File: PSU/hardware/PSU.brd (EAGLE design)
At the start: 143.5 x 58.5 mm, 202 parts, among them J1 SWD, J2 UART, Q1 PMOS-DPAK, Q10 PMOS-SOT23, Q11 NPN, Q2 PMOS-SOT23, Q3 NPN, Q4 PMOS-SOT23, Q5 NMOS-SOT23, Q6 PMOS-DPAK, Q7 PMOS-SOT23, Q8 NMOS-SOT23, Q9 PMOS-DPAK, U1 LM2576, U10 4069, U11 LTV-247, U12 74HC08, U13 STM8S003K3T6C, U14 74HC08, U15 4051, U16 358, U17 358, U18 74HC32, U2 MT3608, U3 7805, U4 324, U5 MC34063, U6 MT3608, U7 LM2576, U8 MC34063, U9 TP4056

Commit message: [HW/PSU] Fix backup regulator enabling
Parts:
- added Q12: PMOS-SOT23, SparkFun-DiscreteSemi:SOT23-3
- moved C12 0.63 mm to (41.3, 47.6)
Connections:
- new net VBACKUP_SW: C12.1, L4.1, Q12.3, U6.4, U6.5
- net MEM_BACKUP: now also Q12.1; no longer U6.4
- net VBACKUP: now also Q12.2; no longer C12.1, L4.1, U6.5
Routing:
- net VBACKUP: track 190.6 -> 175.9 mm, vias 4 -> 3
- net VBACKUP_SW: track 0.00 -> 12.8 mm, vias 0 -> 1
- net MEM_BACKUP: track 21.8 -> 16.5 mm
- net VCCIO: track 181.9 -> 180.4 mm
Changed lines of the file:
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@@
 <attribute name="SPICEPREFIX" value="R" x="46.355" y="19.05" size="0.254" layer="156" font="vector" ratio="10" rot="MR180" display="off"/>
 </element>
-<element name="C12" library="rcl" library_urn="urn:adsk.eagle:library:334" package="C1206" package3d_urn="urn:adsk.eagle:package:23618/2" value="10u" x="40.64" y="47.625" smashed="yes" rot="MR90">
-<attribute name="NAME" x="40.64" y="44.958" size="0.8128" layer="26" font="vector" ratio="10" rot="MR180" align="bottom-center"/>
-<attribute name="POPULARITY" value="54" x="44.45" y="36.195" size="0.254" layer="156" font="vector" ratio="10" rot="MR90" display="off"/>
-<attribute name="SPICEPREFIX" value="C" x="44.45" y="36.195" size="0.254" layer="156" font="vector" ratio="10" rot="MR90" display="off"/>
+<element name="C12" library="rcl" library_urn="urn:adsk.eagle:library:334" package="C1206" package3d_urn="urn:adsk.eagle:package:23618/2" value="10u" x="41.275" y="47.625" smashed="yes" rot="MR90">
+<attribute name="NAME" x="41.275" y="44.958" size="0.8128" layer="26" font="vector" ratio="10" rot="MR180" align="bottom-center"/>
+<attribute name="POPULARITY" value="54" x="45.085" y="36.195" size="0.254" layer="156" font="vector" ratio="10" rot="MR90" display="off"/>
+<attribute name="SPICEPREFIX" value="C" x="45.085" y="36.195" size="0.254" layer="156" font="vector" ratio="10" rot="MR90" display="off"/>
 </element>
 <element name="D9" library="custom" package="DO-214AC" value="SS14" x="52.07" y="46.99" smashed="yes" rot="MR0">
@@
 <attribute name="TP_SIGNAL_NAME" value="" x="48.895" y="18.415" size="0.254" layer="156" font="vector" ratio="10"/>
 </element>
+<element name="Q12" library="SparkFun-DiscreteSemi" package="SOT23-3" value="PMOS-SOT23" x="38.1" y="46.99" smashed="yes" rot="MR180">
+<attribute name="NAME" x="38.1" y="45.085" size="0.8128" layer="26" font="vector" ratio="10" rot="MR180" align="bottom-center"/>
+<attribute name="PROD_ID" value="TRANS-11153" x="38.1" y="46.99" size="1.778" layer="28" rot="MR180" display="off"/>
+<attribute name="VALUE" x="39.751" y="46.99" size="0.6096" layer="28" font="vector" ratio="20" rot="MR270" align="top-center"/>
+</element>
 </elements>
 <signals>
@@
 <contactref element="U9" pad="5"/>
 <contactref element="PJ3" pad="1"/>
-<contactref element="U6" pad="5"/>
-<contactref element="C12" pad="1"/>
 <contactref element="D4" pad="A"/>
 <contactref element="U15" pad="12"/>
 <contactref element="C22" pad="1"/>
-<contactref element="L4" pad="1"/>
-<via x="37.465" y="53.34" extent="1-16" drill="0.35" shape="octagon"/>
-<via x="43.18" y="46.355" extent="1-16" drill="0.35" shape="octagon"/>
-<via x="46.99" y="53.34" extent="1-16" drill="0.35" shape="octagon"/>
 <via x="97.79" y="21.844" extent="1-16" drill="0.35" shape="octagon"/>
-<wire x1="37.465" y1="53.34" x2="46.99" y2="53.34" width="0.4064" layer="16"/>
-<wire x1="46.99" y1="53.34" x2="86.995" y2="53.34" width="0.4064" layer="16"/>
+<wire x1="48.895" y1="53.34" x2="86.995" y2="53.34" width="0.4064" layer="16"/>
 <wire x1="86.995" y1="53.34" x2="89.535" y2="55.88" width="0.4064" layer="16"/>
 <wire x1="89.535" y1="55.88" x2="96.52" y2="55.88" width="0.4064" layer="16"/>
@@
 <wire x1="108.08" y1="45.85" x2="109.22" y2="46.99" width="0.4064" layer="16"/>
 <wire x1="109.22" y1="44.9834" x2="109.22" y2="46.99" width="0.4064" layer="16"/>
-<wire x1="46.355" y1="50.165" x2="43.285" y2="50.165" width="0.4064" layer="1"/>
-<wire x1="43.18" y1="46.355" x2="43.18" y2="50.06" width="0.4064" layer="1"/>
-<wire x1="43.18" y1="50.06" x2="43.285" y2="50.165" width="0.4064" layer="1"/>
-<wire x1="46.355" y1="50.165" x2="46.99" y2="50.8" width="0.4064" layer="1"/>
-<wire x1="46.99" y1="50.8" x2="46.99" y2="53.34" width="0.4064" layer="1"/>
-<wire x1="46.99" y1="53.34" x2="65.405" y2="53.34" width="0.4064" layer="1"/>
+<wire x1="48.895" y1="53.34" x2="65.405" y2="53.34" width="0.4064" layer="1"/>
 <wire x1="65.405" y1="53.34" x2="67.31" y2="51.435" width="0.4064" layer="1"/>
 <wire x1="67.31" y1="51.435" x2="67.31" y2="34.925" width="0.4064" layer="1"/>
@@
 <wire x1="97.79" y1="24.765" x2="97.155" y2="25.4" width="0.4064" layer="1"/>
 <wire x1="88.265" y1="25.4" x2="97.155" y2="25.4" width="0.4064" layer="1"/>
-<wire x1="44.9799" y1="47.625" x2="43.815" y2="47.625" width="0.4064" layer="16"/>
-<wire x1="43.815" y1="47.625" x2="43.18" y2="46.99" width="0.4064" layer="16"/>
-<wire x1="43.18" y1="46.99" x2="43.18" y2="46.355" width="0.4064" layer="16"/>
 <wire x1="97.79" y1="21.844" x2="97.79" y2="24.0284" width="0.4064" layer="16"/>
 <wire x1="69.85" y1="32.385" x2="82.55" y2="32.385" width="0.4064" layer="1"/>
@@
 <wire x1="84.455" y1="28.575" x2="85.09" y2="28.575" width="0.4064" layer="1"/>
 <wire x1="85.09" y1="28.575" x2="88.265" y2="25.4" width="0.4064" layer="1"/>
-<wire x1="40.64" y1="46.225" x2="41.78" y2="46.225" width="0.4064" layer="16"/>
-<wire x1="41.78" y1="46.225" x2="41.91" y2="46.355" width="0.4064" layer="16"/>
-<wire x1="41.91" y1="46.355" x2="43.18" y2="46.355" width="0.4064" layer="16"/>
+<contactref element="Q12" pad="2"/>
+<wire x1="39.05" y1="47.99" x2="39.64" y2="47.99" width="0.4064" layer="16"/>
+<wire x1="39.64" y1="47.99" x2="40.005" y2="47.625" width="0.4064" layer="16"/>
+<wire x1="40.005" y1="47.625" x2="42.545" y2="47.625" width="0.4064" layer="16"/>
+<wire x1="42.545" y1="47.625" x2="43.18" y2="48.26" width="0.4064" layer="16"/>
+<wire x1="43.18" y1="48.26" x2="43.18" y2="48.895" width="0.4064" layer="16"/>
+<wire x1="44.4274" y1="50.1424" x2="48.26" y2="50.1424" width="0.4064" layer="16"/>
+<wire x1="43.18" y1="48.895" x2="44.4274" y2="50.1424" width="0.4064" layer="16"/>
+<via x="48.26" y="50.1424" extent="1-16" drill="0.35" shape="octagon"/>
+<via x="48.895" y="53.34" extent="1-16" drill="0.35" shape="octagon"/>
+<wire x1="48.895" y1="53.34" x2="48.26" y2="52.705" width="0.4064" layer="1"/>
+<wire x1="48.26" y1="52.705" x2="48.26" y2="50.1424" width="0.4064" layer="1"/>
 </signal>
 <signal name="^CHG_CTRL" class="1">
@@
 <contactref element="U10" pad="9"/>
 <wire x1="81.915" y1="26.5684" x2="81.915" y2="27.94" width="0.254" layer="1"/>
-<wire x1="80.645" y1="28.575" x2="80.01" y2="28.575" width="0.254" layer="1"/>
-<wire x1="80.01" y1="28.575" x2="79.375" y2="27.94" width="0.254" layer="1"/>
 <wire x1="79.89" y1="30.48" x2="79.89" y2="29.33" width="0.254" layer="1"/>
 <wire x1="79.89" y1="29.33" x2="80.645" y2="28.575" width="0.254" layer="1"/>
@@
 </signal>
 <signal name="MEM_BACKUP" class="1">
-<contactref element="U6" pad="4"/>
-<wire x1="44.9799" y1="46.675" x2="44.9799" y2="46.2499" width="0.254" layer="16"/>
-<wire x1="43.815" y1="45.085" x2="41.91" y2="45.085" width="0.254" layer="16"/>
-<wire x1="41.91" y1="45.085" x2="41.275" y2="44.45" width="0.254" layer="16"/>
-<wire x1="41.275" y1="44.45" x2="38.1" y2="44.45" width="0.254" layer="16"/>
-<wire x1="38.1" y1="44.45" x2="36.83" y2="43.18" width="0.254" layer="16"/>
-<wire x1="36.83" y1="43.18" x2="35.56" y2="43.18" width="0.254" layer="16"/>
-<wire x1="44.9799" y1="46.2499" x2="43.815" y2="45.085" width="0.254" layer="16"/>
 <contactref element="U12" pad="11"/>
+<wire x1="36.195" y1="43.18" x2="35.56" y2="43.18" width="0.254" layer="16"/>
 <wire x1="32.385" y1="36.0934" x2="32.385" y2="37.465" width="0.254" layer="1"/>
 <wire x1="32.385" y1="37.465" x2="32.385" y2="38.735" width="0.254" layer="1"/>
@@
 <wire x1="33.655" y1="38.1" x2="33.02" y2="38.1" width="0.254" layer="1"/>
 <wire x1="33.02" y1="38.1" x2="32.385" y2="37.465" width="0.254" layer="1"/>
+<contactref element="Q12" pad="1"/>
+<wire x1="37.15" y1="47.99" x2="37.15" y2="46.675" width="0.254" layer="16"/>
+<wire x1="37.15" y1="46.675" x2="36.83" y2="46.355" width="0.254" layer="16"/>
+<wire x1="36.83" y1="46.355" x2="36.83" y2="43.815" width="0.254" layer="16"/>
+<wire x1="36.83" y1="43.815" x2="36.195" y2="43.18" width="0.254" layer="16"/>
 </signal>
 <signal name="MB_SW" class="2">
@@
 <wire x1="64.135" y1="28.575" x2="70.485" y2="28.575" width="0.254" layer="1"/>
 </signal>
+<signal name="VBACKUP_SW" class="2">
+<contactref element="Q12" pad="3"/>
+<contactref element="U6" pad="5"/>
+<contactref element="C12" pad="1"/>
+<contactref element="L4" pad="1"/>
+<contactref element="U6" pad="4"/>
+<via x="43.18" y="46.355" extent="1-16" drill="0.35" shape="octagon"/>
+<wire x1="43.18" y1="46.355" x2="43.18" y2="50.06" width="0.4064" layer="1"/>
+<wire x1="43.18" y1="50.06" x2="43.285" y2="50.165" width="0.4064" layer="1"/>
+<wire x1="44.9799" y1="47.625" x2="43.815" y2="47.625" width="0.4064" layer="16"/>
+<wire x1="43.815" y1="47.625" x2="43.18" y2="46.99" width="0.4064" layer="16"/>
+<wire x1="43.18" y1="46.99" x2="43.18" y2="46.355" width="0.4064" layer="16"/>
+<wire x1="44.9799" y1="46.675" x2="44.9799" y2="47.625" width="0.4064" layer="16"/>
+<wire x1="39.54" y1="45.89" x2="38.1" y2="45.89" width="0.4064" layer="16"/>
+<wire x1="43.18" y1="46.355" x2="41.405" y2="46.355" width="0.4064" layer="16"/>
+<wire x1="41.405" y1="46.355" x2="41.275" y2="46.225" width="0.4064" layer="16"/>
+<wire x1="41.275" y1="46.225" x2="39.875" y2="46.225" width="0.4064" layer="16"/>
+<wire x1="39.875" y1="46.225" x2="39.54" y2="45.89" width="0.4064" layer="16"/>
+</signal>
 </signals>

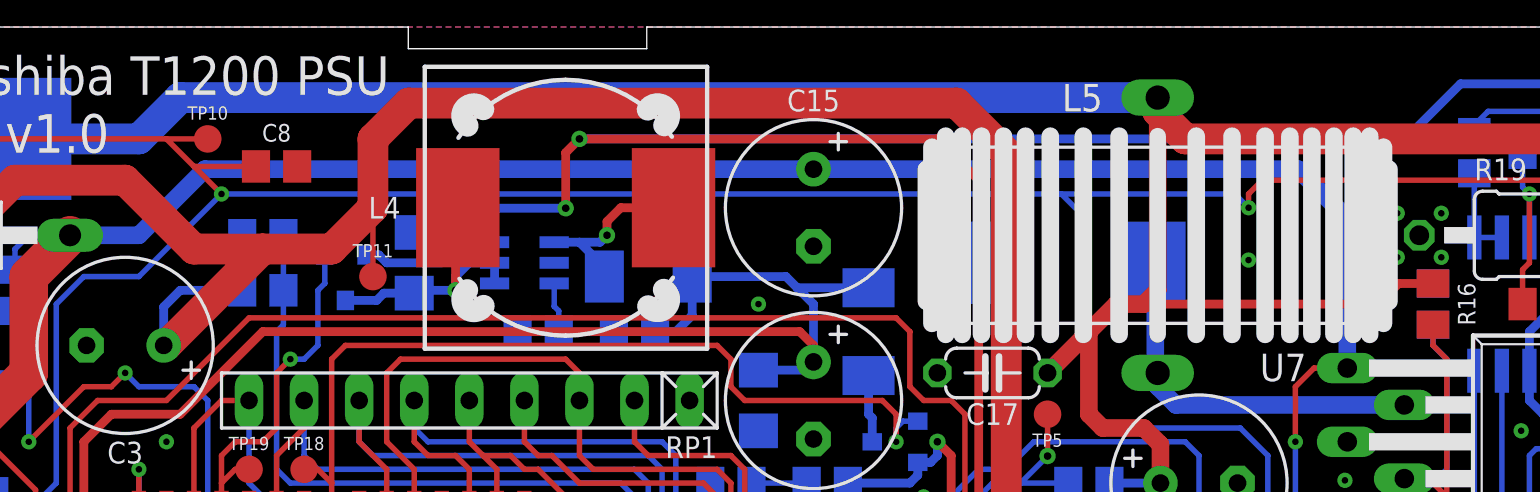
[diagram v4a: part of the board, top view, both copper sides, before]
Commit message: [HW/PSU] Fix backup regulator enabling logic level
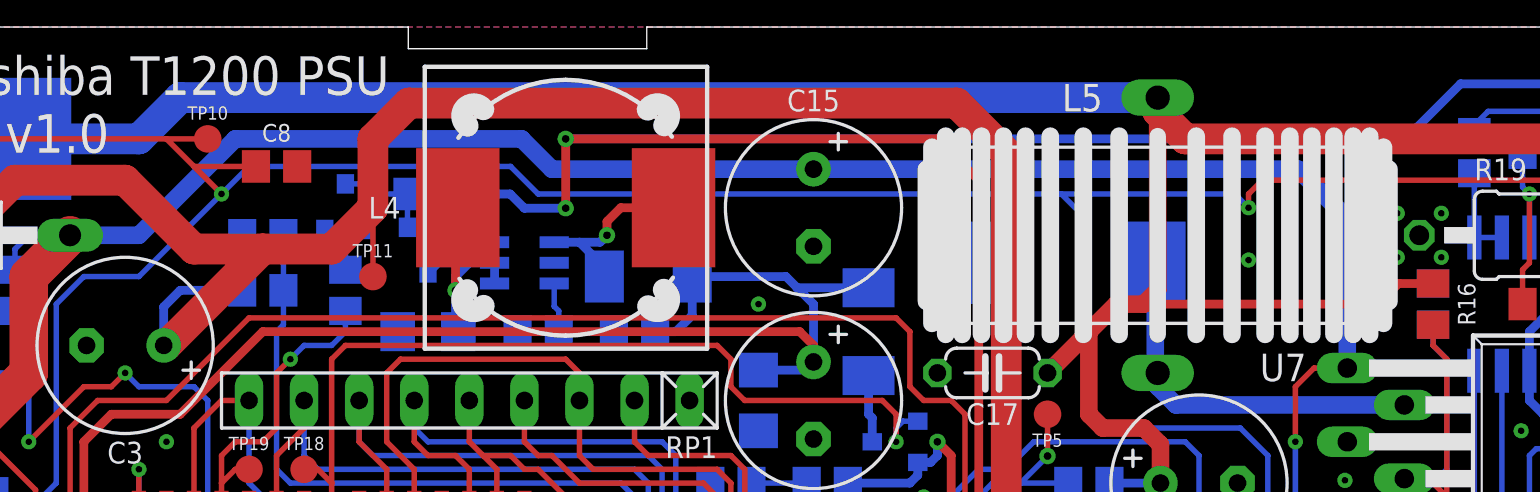
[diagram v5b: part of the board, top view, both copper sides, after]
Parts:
- added Q13: NPN, SparkFun-DiscreteSemi:SOT23-3
- added R77, R78: 10k, rcl:R0805
- moved Q12 4.02 mm to (41.9, 48.3)
- moved C12 3.24 mm to (41.9, 44.5), turned to 0 degrees
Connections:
- new net VBACKUP_SW_B: Q13.1, R78.2
- new net VBACKUP_SW_G: Q12.1, Q13.3, R77.1
- net GND: now also Q13.2
- net MEM_BACKUP: now also R78.1; no longer Q12.1
- net VBACKUP: now also R77.2
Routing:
- net VBACKUP_SW_G: track 0.00 -> 4.59 mm
- net VBACKUP_SW_B: track 0.00 -> 2.65 mm
- net VBACKUP: track 175.9 -> 173.3 mm
- net MEM_BACKUP: track 16.5 -> 14.7 mm
- net VBACKUP_SW: track 12.8 -> 11.6 mm
- net VIN: track 112.7 -> 113.8 mm
- net VCCINT: track 224.3 -> 225.3 mm

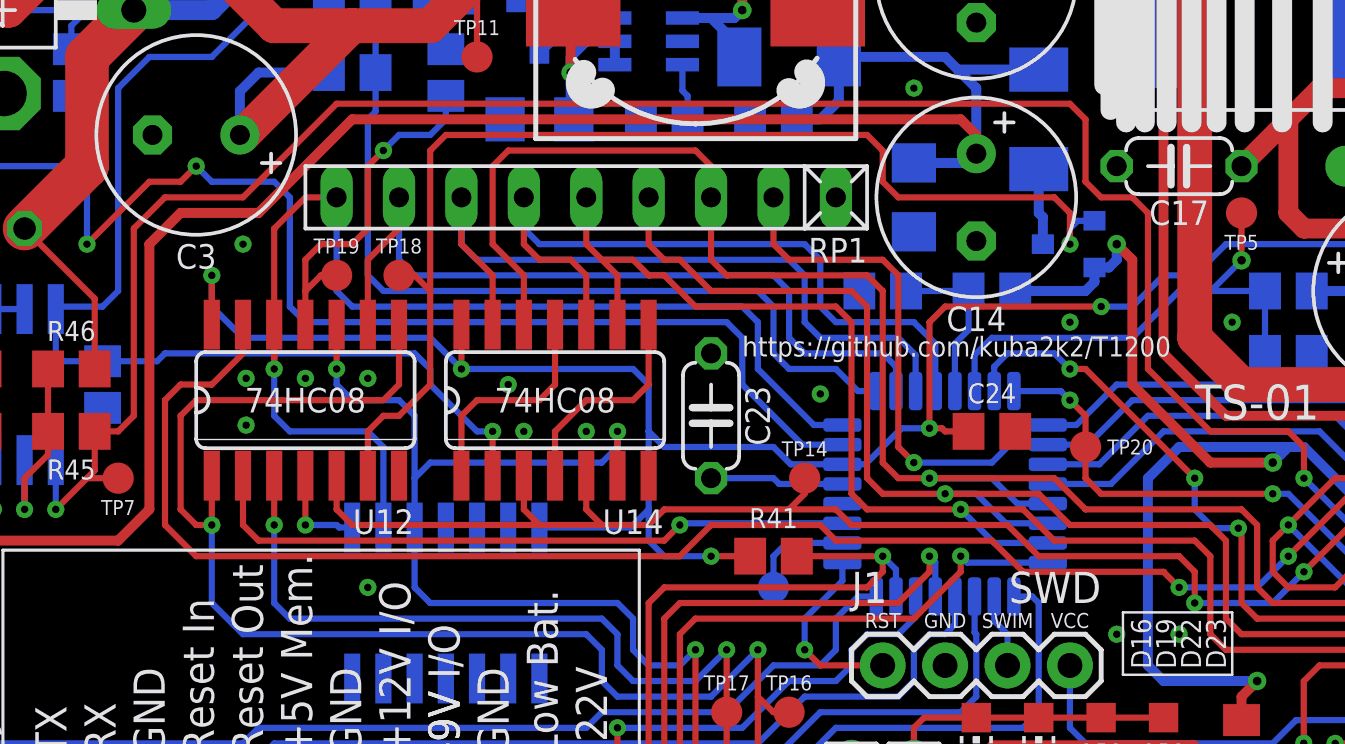
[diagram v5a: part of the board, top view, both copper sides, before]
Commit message: [HW/PSU] Fix +5V_MEM enabling logic level
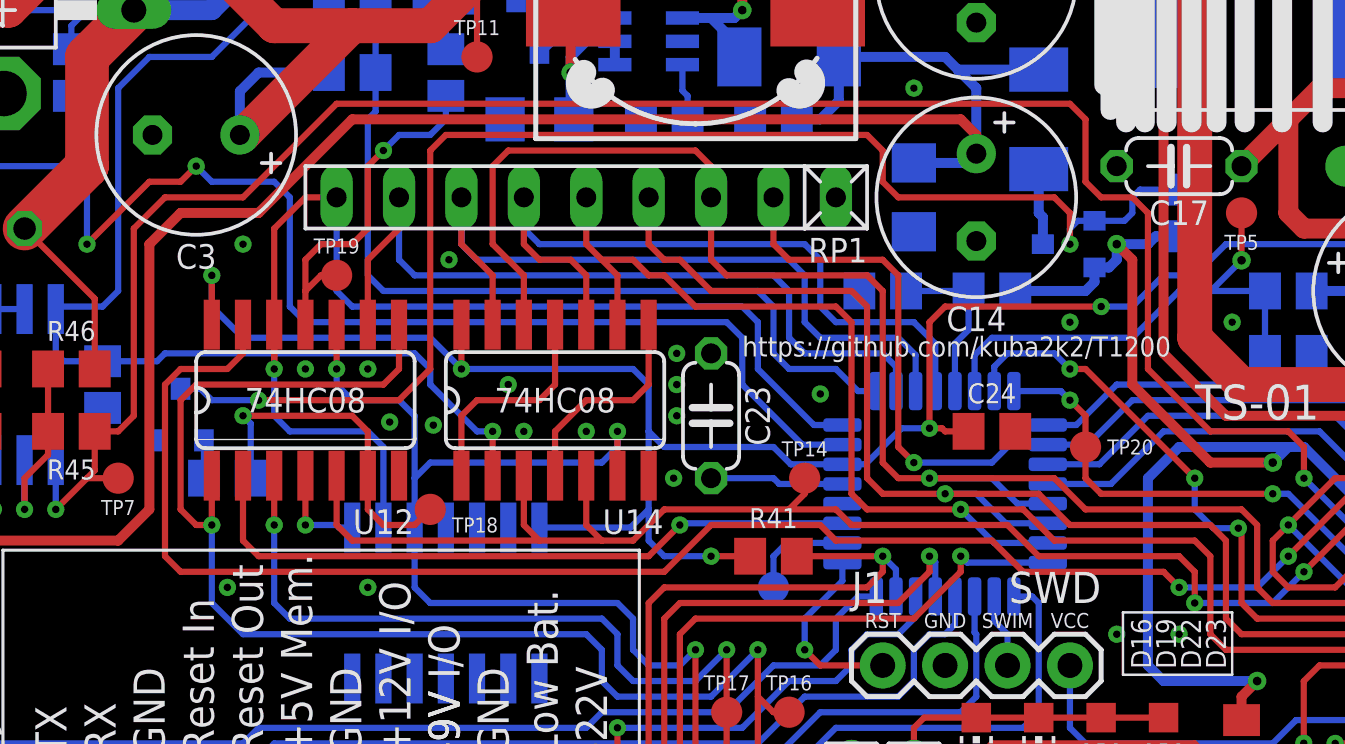
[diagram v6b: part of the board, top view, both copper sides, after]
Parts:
- added Q14: NPN, SparkFun-DiscreteSemi:SOT23-3
- added R79, R80: 10k, rcl:R0805
- moved TP18 9.61 mm to (37.5, 28.6)
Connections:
- new net +5VMEM_B: Q14.1, R80.2
- new net +5VMEM_G: Q14.3, Q4.1, R79.1
- net +5V: now also R79.2
- net GND: now also Q14.2
- net MEM_MAIN: now also R80.1; no longer Q4.1
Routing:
- net +5VMEM_G: track 0.00 -> 55.5 mm, vias 0 -> 2
- net MEM_MAIN: track 47.6 -> 14.3 mm
- net +5V: track 187.8 -> 190.5 mm
- net PRI_OK: track 56.7 -> 58.9 mm
- net MB_MID: track 67.2 -> 68.9 mm
- net +5VMEM_B: track 0.00 -> 1.54 mm
- net HDD12_CTRL: track 27.0 -> 27.9 mm
